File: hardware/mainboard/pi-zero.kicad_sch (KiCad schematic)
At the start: 31 parts, among them J24 Conn_01x05_Pin, J26 USB_A_Stacked, J27 USB_A_Stacked, T1 5V, T1 D+, T1 D-, T1 Gnd, T1 RXD, T1 Shield, T1 TXD, U13 SL2.1S, Y2 12MHz

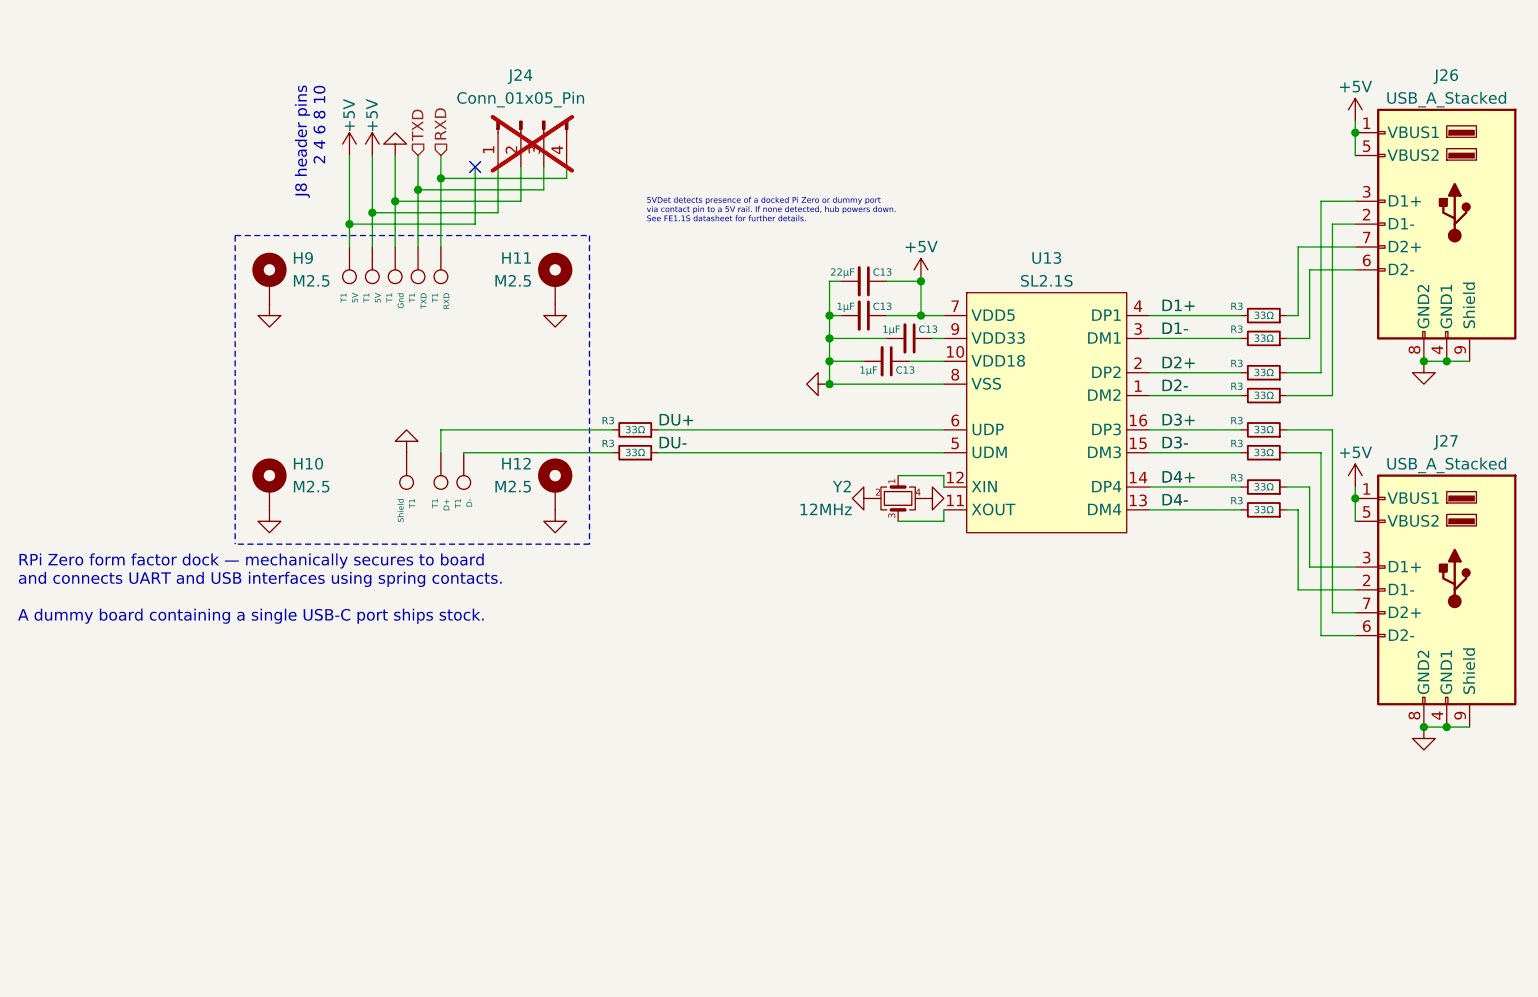
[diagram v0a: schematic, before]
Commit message: added more 3D models and created first few renders
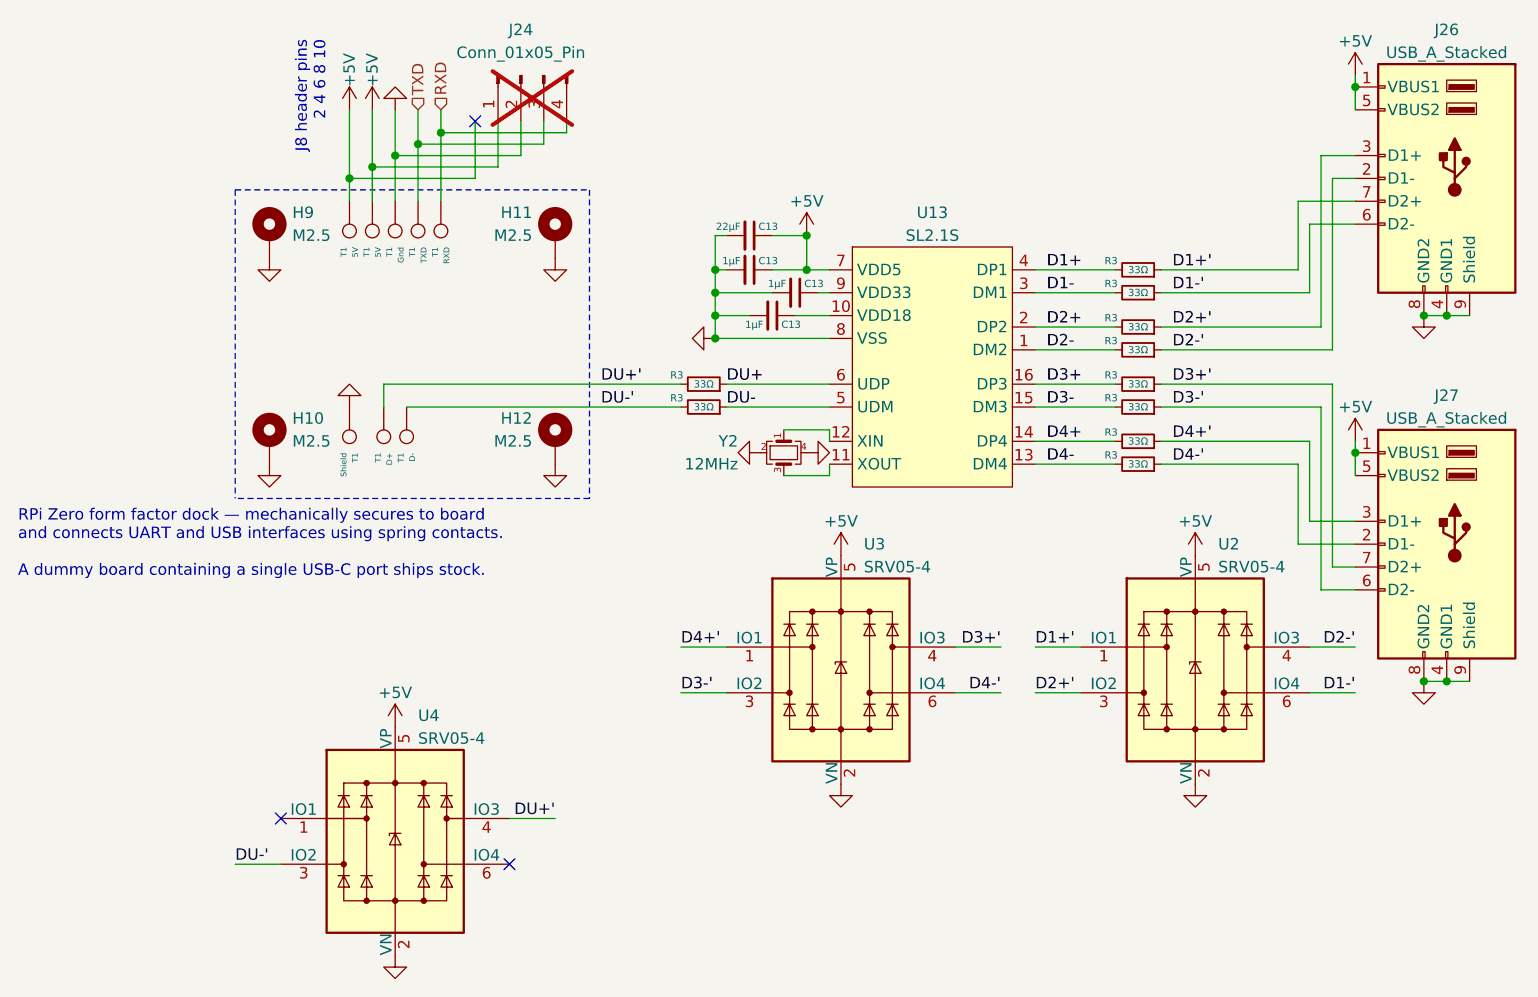
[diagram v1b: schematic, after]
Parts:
- added U2, U3, U4: SRV05-4, Package_TO_SOT_SMD:SOT-23-6, symbol Power_Protection:SRV05-4
- J26, J27: footprint Connector_USB:USB_A_CUI_UJ2-ADH-TH_Horizontal_Stacked -> corevus:USB_Type-A_x2
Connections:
- net +5V: now also U2.5 (VP), U3.5 (VP), U4.5 (VP)
- net GND: now also U2.2 (VN), U3.2 (VN), U4.2 (VN)
- net DU-': now reaches R3.2, T1.1
- net DU-': now also U4.3 (IO2)
- net D3+': now reaches J27.7 (D2+), R3.1
- net D3+': now also U3.4 (IO3)
- net D2-': now reaches J26.2 (D1-), R3.1
- net D2-': now also U2.4 (IO3)
- net D2+': now reaches J26.3 (D1+), R3.1
- net D2+': now also U2.3 (IO2)
- net D1-': now reaches J26.6 (D2-), R3.1
- net D1-': now also U2.6 (IO4)
- net D1+': now reaches J26.7 (D2+), R3.1
- net D1+': now also U2.1 (IO1)
- net D4-': now reaches J27.2 (D1-), R3.1
- net D4-': now also U3.6 (IO4)
- net D4+': now reaches J27.3 (D1+), R3.1
- net D4+': now also U3.1 (IO1)
- net D3-': now reaches J27.6 (D2-), R3.1
- net D3-': now also U3.3 (IO2)
- net DU+': now reaches R3.2, T1.1
- net DU+': now also U4.4 (IO3)
- no-connect marks 1 -> 3
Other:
- note removed: "5VDet detects presence of a docked Pi Zero or dummy port via contact pin to a 5V rail. If none detected, hub powers down. See FE1.1S datasheet for further details."
- moved on the sheet: C13, H10, H11, H12, H9, J24, J26, J27, R3, T1, U13, Y2
